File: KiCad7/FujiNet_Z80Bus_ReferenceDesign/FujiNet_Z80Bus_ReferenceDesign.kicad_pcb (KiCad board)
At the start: 2 copper layers, 180 x 120 mm, 59 parts, among them IC1 74HC32N, IC2 74HC590N, IC3 74HC590N, J1 DIAG-HOST_SYSTEM_BUS, J3 Logic core connector

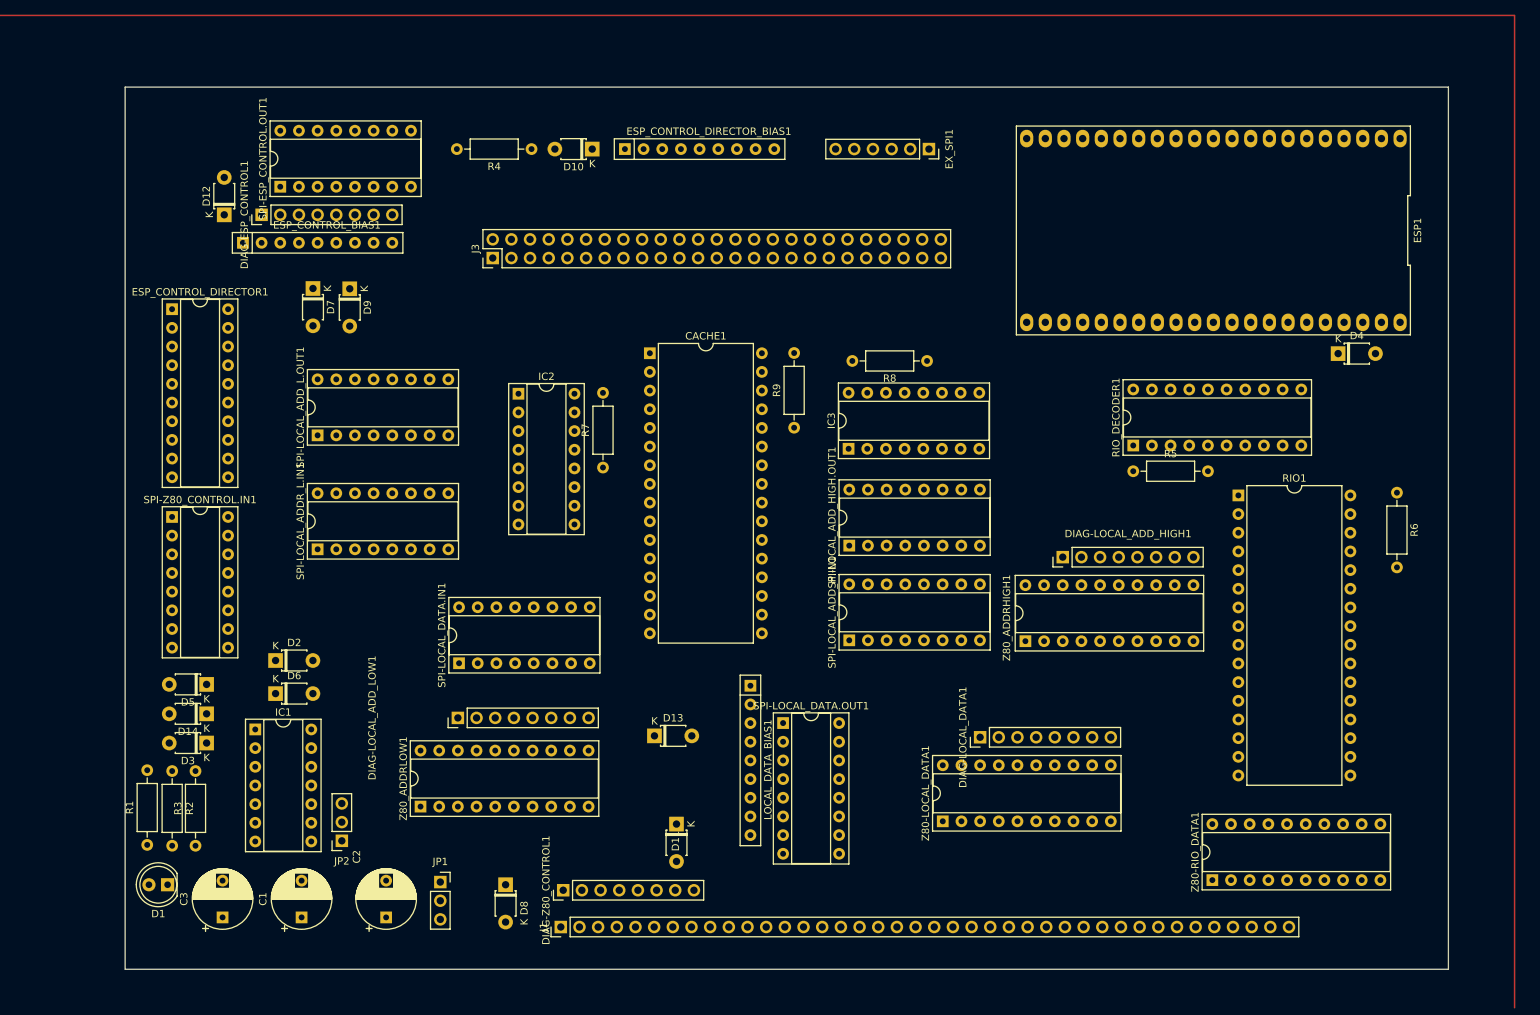
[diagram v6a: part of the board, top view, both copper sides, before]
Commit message: KiCad - Proof of concept PCB in-progress
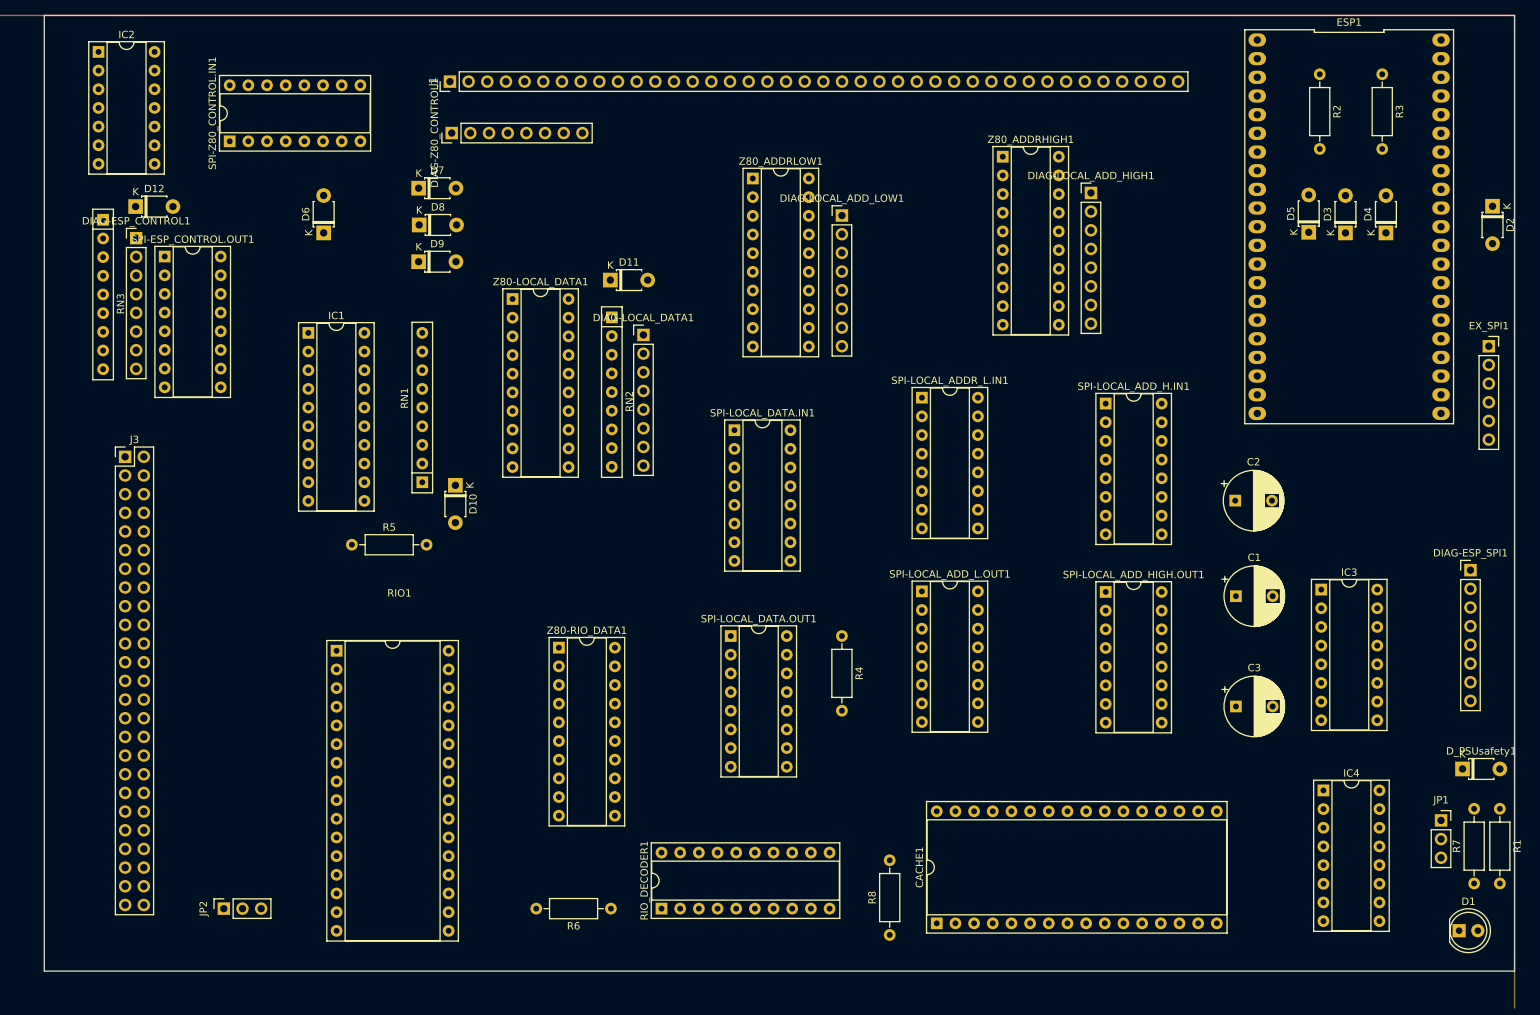
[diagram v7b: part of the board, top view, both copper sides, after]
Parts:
- removed D13, D14: 1N4148, Diode_THT:D_T-1_P5.08mm_Horizontal
- removed ESP_CONTROL_BIAS1, ESP_CONTROL_DIRECTOR_BIAS1, LOCAL_DATA_BIAS1: 4609M-101-103LF, Resistor_THT:R_Array_SIP9
- removed ESP_CONTROL_DIRECTOR1: 74HC244N, Package_DIP:DIP-20_W7.62mm_Socket
- removed R9: 10K, Resistor_THT:R_Axial_DIN0207_L6.3mm_D2.5mm_P10.16mm_Horizontal
- added DIAG-ESP_SPI1: PinHeader_2.54mm, Connector_PinHeader_2.54mm:PinHeader_1x08_P2.54mm_Vertical, F.Cu at (258.0, 105.5)
- added D_PSUsafety1: 1N4148, Diode_THT:D_T-1_P5.08mm_Horizontal, F.Cu at (256.9, 132.5)
- added IC4: 74HC590N, Package_DIP:DIP-16_W7.62mm_Socket, F.Cu at (238.0, 135.4)
- added RN1: LOCAL_CONTROL_BIAS, Resistor_THT:R_Array_SIP9, F.Cu at (115.4, 93.5)
- added RN2: 4609M-101-103LF, Resistor_THT:R_Array_SIP9, F.Cu at (141.2, 71.1)
- added RN3: 4609M-101-103LF, Resistor_THT:R_Array_SIP9, F.Cu at (72.0, 57.8)
- CACHE1, RIO1: footprint Package_DIP:DIP-32_W15.24mm -> Package_DIP:DIP-32_W15.24mm_Socket
- IC1: value 74HC32N -> 74HC244N; footprint Package_DIP:DIP-14_W7.62mm_Socket -> Package_DIP:DIP-20_W7.62mm_Socket
- IC2: value 74HC590N -> 74HC32N; footprint Package_DIP:DIP-16_W7.62mm_Socket -> Package_DIP:DIP-14_W7.62mm_Socket
- R2: value R10K -> 22K
- R5: value 22K -> 10K
- moved R3 192.5 mm to (246.0, 38.0), turned to -90 degrees
- moved R1 184.1 mm to (262.0, 137.9), turned to -90 degrees
- moved R2 182.6 mm to (237.5, 38.0)
- moved D2 176.7 mm to (261.0, 56.0), turned to -90 degrees
- moved D1 175.8 mm to (256.5, 154.5), turned to 0 degrees
- moved D3 169.8 mm to (241.0, 59.6), turned to 90 degrees
- moved D5 162.0 mm to (236.0, 59.5), turned to 90 degrees
- moved C3 140.8 mm to (226.1, 124.0), turned to 0 degrees
- moved JP1 136.4 mm to (254.0, 139.5)
- moved C1 134.4 mm to (226.1, 109.0), turned to 0 degrees
- moved R7 131.3 mm to (258.5, 148.1)
- moved C2 128.7 mm to (226.0, 96.0), turned to 0 degrees
- moved RIO1 124.5 mm to (103.8, 116.4)
- moved R6 121.0 mm to (141.1, 151.5), turned to 180 degrees
- moved J1 116.0 mm to (119.2, 39.0)
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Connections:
- D10 pad 1: /ESP_CONTROL.ROMCS -> Net-(D10-K)
- D10 pad 2: /Z80_CONTROL.ROMCS -> +5V
- D11 pad 1: /ESP_CONTROL.NMI -> Net-(D11-K)
- D11 pad 2: /Z80_CONTROL.NMI -> +5V
- D2 pad 2: /CORE_ESP32-WROVER/ESP_PULSE -> /Z80_CONTROL.RESET
- D3 pad 1: Net-(D2-K) -> /Z80_CONTROL.WAIT
- D3 pad 2: /ESP_CONTROL.WR -> /CORE_ESP32-WROVER/ESP_INT
- D4 pad 1: Net-(D4-K) -> /Z80_HARDLOCK_RESET
- D4 pad 2: /Z80_CONTROL.RESET -> /CORE_ESP32-WROVER/ESP_INT
- D5 pad 1: /Z80_CONTROL.WAIT -> /Z80_CONTROL.BUSACK
- D6 pad 1: /Z80_HARDLOCK_RESET -> /ESP_CONTROL.NMI
- D6 pad 2: /CORE_ESP32-WROVER/ESP_INT -> /Z80_CONTROL.NMI
- D7 pad 1: /Z80_CONTROL.BUSACK -> /ESP_CONTROL.ROMCS
- D7 pad 2: /CORE_ESP32-WROVER/ESP_INT -> /Z80_CONTROL.ROMCS
- D8 pad 1: /ESP_CONTROL.BUSRQ -> /ESP_CONTROL.WAIT
- D8 pad 2: /Z80_CONTROL.BUSRQ -> /Z80_CONTROL.WAIT
- D9 pad 1: /ESP_CONTROL.WAIT -> /ESP_CONTROL.BUSRQ
- D9 pad 2: /Z80_CONTROL.WAIT -> /Z80_CONTROL.BUSRQ
- ESP1 pad 26: /!ESP_HARDLOCK -> /ESP_HARDLOCK
- ESP1 pad 35: Net-(D4-K) -> Net-(D2-K)
- IC1 pad 1: GND -> /ESP_CONTROL.BUSRQ
- IC1 pad 11: /CORE_ESP32-WROVER/ESP_CONTROL.WR+ESP_PULSE -> /ESP_CONTROL.MEMRQ
- IC1 pad 12: /CORE_ESP32-WROVER/ESP_PULSE -> /LOCAL_CONTROL.MEMRQ
- IC1 pad 13: /ESP_CONTROL.WR -> /ESP_CONTROL.IORQ
- IC1 pad 14: +5V -> /LOCAL_CONTROL.IORQ
- IC1 pad 2: GND -> /ESP_CONTROL.RD
- IC1 pad 3: unconnected-(IC1-Pad3) -> /Z80_CONTROL.RD
- IC1 pad 4: GND -> /SPI-Z80-BUS_ZXspectrum/ESP_CONTROL.WR+ESP_PULSE
- IC1 pad 5: GND -> /Z80_CONTROL.WR
- IC1 pad 6: unconnected-(IC1-Pad6) -> /ESP_CONTROL.IORQ
- IC1 pad 7: GND -> /Z80_CONTROL.IORQ
- IC1 pad 8: unconnected-(IC1-Pad8) -> /ESP_CONTROL.MEMRQ
- IC1 pad 9: GND -> /Z80_CONTROL.MEMRQ
- IC2 pad 1: /LOCAL_A1 -> /CORE_ESP32-WROVER/ESP_PULSE
- IC2 pad 10: /Z80_HARDLOCK -> GND
- IC2 pad 11: /CACHE_CONTROL.DATASTATUS+PERM_Z80_IORQ -> unconnected-(IC2-Pad11)
- IC2 pad 12: /CACHE_DATASTATUS -> GND
- IC2 pad 13: /CACHE_CONTROL.DATASTATUS+PERM_Z80_IORQ -> GND
- IC2 pad 14: /CACHE_DATASTATUS -> +5V
- IC2 pad 2: /LOCAL_A2 -> /ESP_CONTROL.WR
- IC2 pad 3: /LOCAL_A3 -> /SPI-Z80-BUS_ZXspectrum/ESP_CONTROL.WR+ESP_PULSE
- IC2 pad 4: /LOCAL_A4 -> GND
- IC2 pad 5: /LOCAL_A5 -> GND
- IC2 pad 6: /LOCAL_A6 -> unconnected-(IC2-Pad6)
- IC2 pad 7: /LOCAL_A7 -> GND
- IC2 pad 8: GND -> unconnected-(IC2-Pad8)
- IC2 pad 9: Net-(IC2-~{RCO}) -> GND
- IC3 pad 1: /LOCAL_A9 -> /LOCAL_A1
- IC3 pad 11: Net-(IC2-~{RCO}) -> /CACHE_CONTROL.DATASTATUS+PERM_Z80_IORQ
- IC3 pad 13: Net-(IC2-~{RCO}) -> /CACHE_CONTROL.DATASTATUS+PERM_Z80_IORQ
- IC3 pad 15: /LOCAL_A8 -> /LOCAL_A0
- IC3 pad 2: /LOCAL_A10 -> /LOCAL_A2
- IC3 pad 3: /LOCAL_A11 -> /LOCAL_A3
- IC3 pad 4: unconnected-(IC3-Q4-Pad4) -> /LOCAL_A4
- IC3 pad 5: unconnected-(IC3-Q5-Pad5) -> /LOCAL_A5
- IC3 pad 6: unconnected-(IC3-Q6-Pad6) -> /LOCAL_A6
- IC3 pad 7: unconnected-(IC3-Q7-Pad7) -> /LOCAL_A7
- IC3 pad 9: unconnected-(IC3-~{RCO}-Pad9) -> Net-(IC3-~{RCO})
- J1 pad 11: /Z80_A0 -> /Z80_D0
- J1 pad 12: /Z80_A1 -> /Z80_D1
- J1 pad 13: /Z80_A2 -> /Z80_D2
- J1 pad 14: /Z80_A3 -> /Z80_D3
- J1 pad 15: /Z80_A4 -> /Z80_D4
- J1 pad 16: /Z80_A5 -> /Z80_D5
- J1 pad 17: /Z80_A6 -> /Z80_D6
- J1 pad 18: /Z80_A7 -> /Z80_D7
- J1 pad 19: /Z80_A8 -> /Z80_A0
- J1 pad 20: /Z80_A9 -> /Z80_A1
- J1 pad 21: /Z80_A10 -> /Z80_A2
- J1 pad 22: /Z80_A11 -> /Z80_A3
- J1 pad 23: /Z80_A12 -> /Z80_A4
- J1 pad 24: /Z80_A13 -> /Z80_A5
- J1 pad 25: /Z80_A14 -> /Z80_A6
- J1 pad 26: /Z80_A15 -> /Z80_A7
- J1 pad 27: /Z80_D0 -> /Z80_A8
- J1 pad 28: /Z80_D1 -> /Z80_A9
- J1 pad 29: /Z80_D2 -> /Z80_A10
- J1 pad 30: /Z80_D3 -> /Z80_A11
- J1 pad 31: /Z80_D4 -> /Z80_A12
- J1 pad 32: /Z80_D5 -> /Z80_A13
- J1 pad 33: /Z80_D6 -> /Z80_A14
- J1 pad 34: /Z80_D7 -> /Z80_A15
- R2 pad 1: Net-(D2-K) -> /CORE_ESP32-WROVER/ESP_INT
- R2 pad 2: GND -> +5V
- R3 pad 1: /CORE_ESP32-WROVER/ESP_INT -> GND
- R3 pad 2: +5V -> /CORE_ESP32-WROVER/ESP_INT
- R4 pad 1: GND -> +5V
- R4 pad 2: /CORE_ESP32-WROVER/ESP_INT -> /CORE_ESP32-WROVER/ESP_SPI_INT.MR
- R5 pad 2: /CORE_ESP32-WROVER/ESP_SPI_INT.MR -> /RIO-128K_ZXspectrum/RIO_CE2
- R6 pad 1: +5V -> Net-(RIO_DECODER1-A->B)
- R6 pad 2: /RIO-128K_ZXspectrum/RIO_CE2 -> +5V
- R7 pad 1: Net-(RIO_DECODER1-A->B) -> /CACHE_DATASTATUS
- R8 pad 1: /CACHE_DATASTATUS -> /IOCACHE-128K_ZXspectrum/CACHE_CE2
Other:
- board size 180 x 120 mm -> 200 x 130 mm

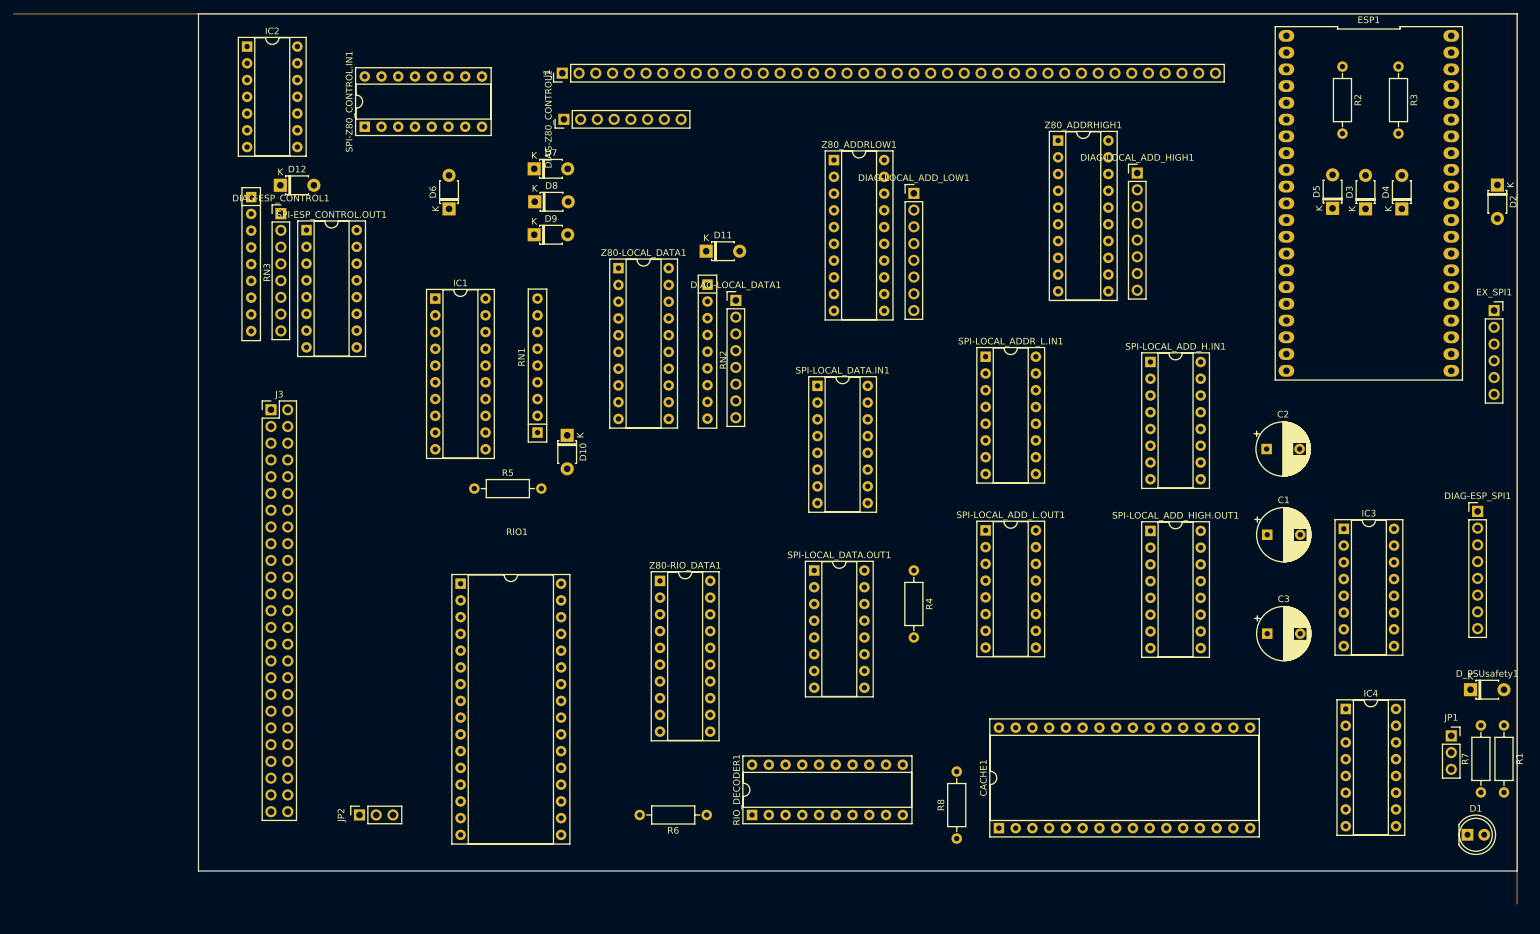
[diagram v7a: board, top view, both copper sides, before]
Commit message: KiCad Prototype routing (failed)
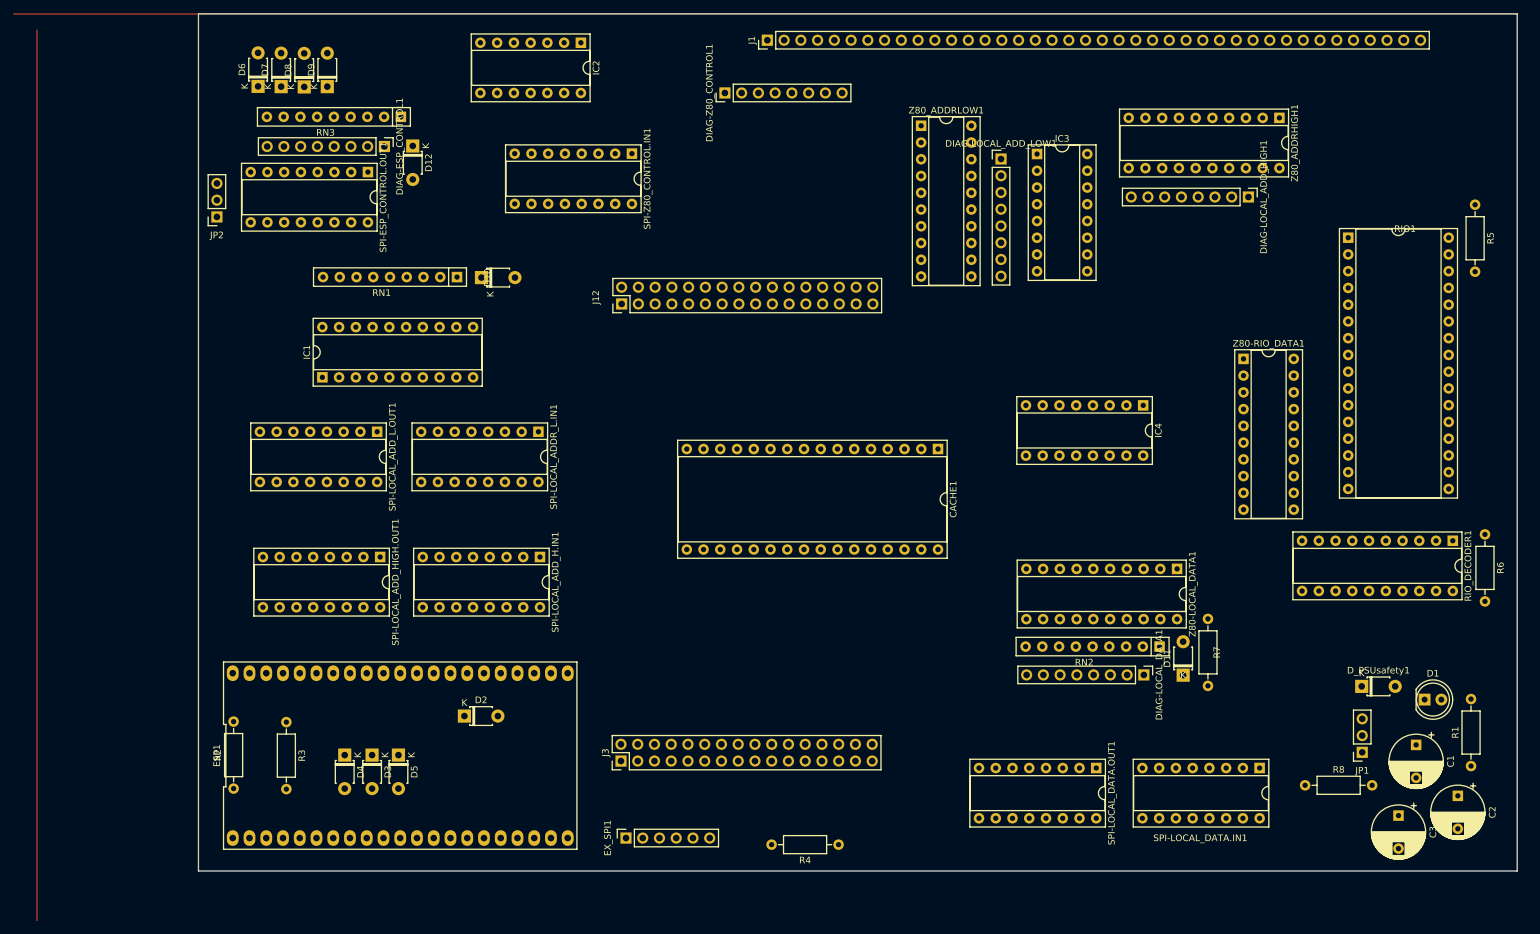
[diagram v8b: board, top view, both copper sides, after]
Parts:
- removed DIAG-ESP_SPI1: PinHeader_2.54mm, Connector_PinHeader_2.54mm:PinHeader_1x08_P2.54mm_Vertical
- added J12: Conn_02x12_Odd_Even, Connector_PinHeader_2.54mm:PinHeader_2x16_P2.54mm_Vertical, F.Cu at (128.2, 74.0)
- J3: value Logic core connector -> Conn_02x12_Odd_Even; footprint Connector_PinHeader_2.54mm:PinHeader_2x25_P2.54mm_Vertical -> Connector_PinHeader_2.54mm:PinHeader_2x16_P2.54mm_Vertical
- moved R2 200.7 mm to (69.3, 147.5), turned to 90 degrees
- moved R3 195.8 mm to (77.3, 137.4)
- moved D4 180.5 mm to (86.2, 142.4), turned to -90 degrees
- moved D2 176.2 mm to (104.3, 136.5), turned to 0 degrees
- moved D3 171.9 mm to (90.3, 142.4), turned to -90 degrees
- moved ESP1 170.8 mm to (93.3, 142.5), turned to 90 degrees
- moved D5 164.2 mm to (94.3, 142.4), turned to -90 degrees
- moved R5 157.8 mm to (257.6, 59.0), turned to -90 degrees
- moved EX_SPI1 154.1 mm to (128.8, 155.0), turned to 90 degrees
- moved RIO1 144.5 mm to (238.4, 64.0)
- moved R6 125.5 mm to (259.1, 109.0), turned to -90 degrees
- moved SPI-LOCAL_ADD_HIGH.OUT1 116.9 mm to (91.6, 112.4), turned to -90 degrees
- moved RIO_DECODER1 114.1 mm to (254.2, 109.9), turned to -90 degrees
- moved SPI-LOCAL_ADD_H.IN1 97.2 mm to (115.8, 112.4), turned to -90 degrees
- moved D11 96.8 mm to (213.3, 130.3), turned to 90 degrees
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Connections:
- J1 pad 11: /Z80_D0 -> /Z80_A7
- J1 pad 12: /Z80_D1 -> /Z80_A6
- J1 pad 13: /Z80_D2 -> /Z80_A5
- J1 pad 14: /Z80_D3 -> /Z80_A4
- J1 pad 15: /Z80_D4 -> /Z80_A3
- J1 pad 16: /Z80_D5 -> /Z80_A2
- J1 pad 17: /Z80_D6 -> /Z80_A1
- J1 pad 18: /Z80_D7 -> /Z80_A0
- J1 pad 19: /Z80_A0 -> /Z80_A15
- J1 pad 20: /Z80_A1 -> /Z80_A14
- J1 pad 21: /Z80_A2 -> /Z80_A13
- J1 pad 22: /Z80_A3 -> /Z80_A12
- J1 pad 23: /Z80_A4 -> /Z80_A11
- J1 pad 24: /Z80_A5 -> /Z80_A10
- J1 pad 25: /Z80_A6 -> /Z80_A9
- J1 pad 26: /Z80_A7 -> /Z80_A8
- J1 pad 27: /Z80_A8 -> /Z80_D0
- J1 pad 28: /Z80_A9 -> /Z80_D1
- J1 pad 29: /Z80_A10 -> /Z80_D2
- J1 pad 30: /Z80_A11 -> /Z80_D3
- J1 pad 31: /Z80_A12 -> /Z80_D4
- J1 pad 32: /Z80_A13 -> /Z80_D5
- J1 pad 33: /Z80_A14 -> /Z80_D6
- J1 pad 34: /Z80_A15 -> /Z80_D7
- J3 pad 1: /Z80_CONTROL.RD -> /IORQ_FILTER_BIT
- J3 pad 10: /ESP_CONTROL.BUSRQ -> /CACHE_CONTROL.DATASTATUS+PERM_Z80_IORQ
- J3 pad 11: /ESP_CONTROL.ROMCS -> /ESP_WAIT_RESET
- J3 pad 12: /LOCAL_CONTROL.RD -> /CACHE_CONTROL.A16
- J3 pad 13: /LOCAL_CONTROL.WR -> /Z80_A15
- J3 pad 14: /LOCAL_CONTROL.IORQ -> /CACHE_CONTROL.WE
- J3 pad 15: /LOCAL_CONTROL.MEMRQ -> /Z80_A14
- J3 pad 16: /Z80_BUS_CONTROL.Z80_ADD_OE -> /CACHE_CONTROL.OE
- J3 pad 17: /Z80_BUS_CONTROL.Z80_ADD_DIR -> /RIO_CONTROL.A14
- J3 pad 18: /Z80_BUS_CONTROL.Z80_DATA_DIR -> /CACHE_CONTROL.CS
- J3 pad 19: /Z80_BUS_CONTROL.Z80_DATA_OE -> /RIO_CONTROL.A15
- J3 pad 2: /Z80_CONTROL.WR -> /Z80_BUS_CONTROL.Z80_ADD_OE
- J3 pad 20: /CACHE_CONTROL.DATASTATUS+PERM_Z80_IORQ -> /Z80_HARDLOCK
- J3 pad 21: /CACHE_CONTROL.A16 -> /RIO_CONTROL.WE
- J3 pad 22: /CACHE_CONTROL.WE -> /!Z80_HARDLOCK
- J3 pad 23: /CACHE_CONTROL.OE -> /RIO_CONTROL.OE
- J3 pad 24: /CACHE_CONTROL.CS -> /PERM_Z80_IORQ
- J3 pad 25: unconnected-(J3-Pin_25-Pad25) -> (no net)
- J3 pad 26: /ESP_ROM_WR_PROTECT -> (no net)
- J3 pad 27: /ESP_ROMSEL_0 -> (no net)
- J3 pad 28: /ESP_ROMSEL_1 -> (no net)
- J3 pad 29: /ESP_HARDLOCK -> (no net)
- J3 pad 3: /Z80_CONTROL.IORQ -> /Z80_HARDLOCK_RESET
- J3 pad 30: /!ESP_HARDLOCK -> (no net)
- J3 pad 31: /Z80_HARDLOCK -> (no net)
- J3 pad 32: /!Z80_HARDLOCK -> (no net)
- J3 pad 4: /Z80_CONTROL.MEMRQ -> /Z80_BUS_CONTROL.Z80_ADD_DIR
- J3 pad 5: /Z80_CONTROL.BUSRQ -> /Z80_HARDLOCK_SET
- J3 pad 6: /Z80_CONTROL.WAIT -> /Z80_BUS_CONTROL.Z80_DATA_DIR
- J3 pad 7: /ESP_CONTROL.WR -> /WAIT_IO
- J3 pad 8: /ESP_CONTROL.IORQ -> /Z80_BUS_CONTROL.Z80_DATA_OE
- J3 pad 9: /ESP_CONTROL.MEMRQ -> /CACHE_DATASTATUS
